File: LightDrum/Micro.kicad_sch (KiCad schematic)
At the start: 14 parts, among them J902 JTAG, SW902 BOOT0, U901 24LC04, Y901 16MHz

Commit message: Add RTC
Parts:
- added C1, C2: 15pF, Capacitor_SMD:C_0402_1005Metric, symbol Daxxn_Device:C
- added Y32: 32.768KHz, Crystal:Crystal_SMD_3215-2Pin_3.2x1.5mm, symbol Daxxn_Device:Crystal_Floating
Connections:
- net GND: now also C1.2, C2.1
- net at STM101.8 (PC14/OSC32-IN): now also C1.1, Y32.1
- net at STM101.9 (PC15/OSC32-OUT): now also C2.2, Y32.2
- no-connect marks 26 -> 24
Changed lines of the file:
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@@
   (junction (at 53.34 93.98) (diameter 0) (color 0 0 0 0)
   )
+  (junction (at 156.21 67.31) (diameter 0) (color 0 0 0 0)
+  )
   (junction (at 49.53 91.44) (diameter 0) (color 0 0 0 0)
   )
+  (junction (at 156.21 72.39) (diameter 0) (color 0 0 0 0)
+  )
   (junction (at 256.54 152.4) (diameter 0) (color 0 0 0 0)
   )
   (junction (at 262.89 71.12) (diameter 0) (color 0 0 0 0)
+  )
+  (junction (at 168.91 72.39) (diameter 0) (color 0 0 0 0)
   )
   (no_connect (at 129.54 78.74))
@@
   (no_connect (at 86.36 60.96))
   (no_connect (at 86.36 71.12))
-  (no_connect (at 129.54 71.12))
   (no_connect (at 86.36 134.62))
   (no_connect (at 86.36 137.16))
@@
   (no_connect (at 129.54 81.28))
   (no_connect (at 129.54 127))
-  (no_connect (at 129.54 68.58))
   (no_connect (at 129.54 33.02))
   (polyline (pts (xy 284.48 134.62) (xy 208.28 134.62))
@@
     (stroke (width 0) (type default))
   )
+  (wire (pts (xy 156.21 67.31) (xy 162.56 67.31))
+    (stroke (width 0) (type default))
+  )
   (wire (pts (xy 233.68 153.67) (xy 233.68 152.4))
     (stroke (width 0) (type default))
@@
     (stroke (width 0) (type default))
   )
+  (wire (pts (xy 129.54 68.58) (xy 149.86 68.58))
+    (stroke (width 0) (type default))
+  )
   (wire (pts (xy 262.89 69.85) (xy 262.89 71.12))
     (stroke (width 0) (type default))
@@
     (stroke (width 0) (type default))
   )
+  (wire (pts (xy 149.86 72.39) (xy 149.86 71.12))
+    (stroke (width 0) (type default))
+  )
   (wire (pts (xy 242.57 101.6) (xy 243.84 101.6))
     (stroke (width 0) (type default))
@@
     (stroke (width 0) (type default))
   )
+  (wire (pts (xy 168.91 72.39) (xy 167.64 72.39))
+    (stroke (width 0) (type default))
+  )
   (wire (pts (xy 255.27 149.86) (xy 256.54 149.86))
     (stroke (width 0) (type default))
@@
     (stroke (width 0) (type default))
   )
+  (wire (pts (xy 168.91 67.31) (xy 168.91 72.39))
+    (stroke (width 0) (type default))
+  )
   (wire (pts (xy 220.98 34.29) (xy 232.41 34.29))
     (stroke (width 0) (type default))
@@
     (stroke (width 0) (type default))
   )
+  (wire (pts (xy 167.64 67.31) (xy 168.91 67.31))
+    (stroke (width 0) (type default))
+  )
   (wire (pts (xy 86.36 101.6) (xy 83.82 101.6))
     (stroke (width 0) (type default))
@@
     (stroke (width 0) (type default))
   )
+  (wire (pts (xy 149.86 68.58) (xy 149.86 67.31))
+    (stroke (width 0) (type default))
+  )
+  (wire (pts (xy 156.21 72.39) (xy 162.56 72.39))
+    (stroke (width 0) (type default))
+  )
+  (wire (pts (xy 168.91 72.39) (xy 168.91 73.66))
+    (stroke (width 0) (type default))
+  )
   (wire (pts (xy 256.54 157.48) (xy 245.11 157.48))
     (stroke (width 0) (type default))
@@
     (stroke (width 0) (type default))
   )
+  (wire (pts (xy 156.21 72.39) (xy 149.86 72.39))
+    (stroke (width 0) (type default))
+  )
   (polyline (pts (xy 208.28 16.51) (xy 236.22 16.51))
     (stroke (width 0) (type default))
@@
     (stroke (width 0) (type default))
   )
+  (wire (pts (xy 149.86 71.12) (xy 129.54 71.12))
+    (stroke (width 0) (type default))
+  )
   (polyline (pts (xy 208.28 86.36) (xy 246.38 86.36))
     (stroke (width 0) (type default))
@@
   )
   (wire (pts (xy 49.53 83.82) (xy 49.53 85.09))
+    (stroke (width 0) (type default))
+  )
+  (wire (pts (xy 149.86 67.31) (xy 156.21 67.31))
     (stroke (width 0) (type default))
   )
@@
     )
   )
+  (symbol (lib_id "Daxxn_Device:C") (at 165.1 72.39 270) (unit 1)
+    (in_bom yes) (on_board yes) (dnp no)
+    (property "Reference" "C2" (at 166.624 72.644 0)
+      (effects (font (size 1.27 1.27)) (justify left))
+    )
+    (property "Value" "15pF" (at 163.195 72.644 0)
+      (effects (font (size 1.27 1.27)) (justify left))
+    )
+    (property "Footprint" "Capacitor_SMD:C_0402_1005Metric" (at 165.1 72.39 0)
+      (effects (font (size 1.27 1.27)) hide)
+    )
+    (property "Datasheet" "~" (at 165.1 72.39 0)
+      (effects (font (size 1.27 1.27)) hide)
+    )
+    (property "Schematic" "" (at 165.1 72.39 0)
+      (effects (font (size 1.27 1.27)) hide)
+    )
+    (property "PartNumber" "" (at 165.1 72.39 0)
+      (effects (font (size 1.27 1.27)))
+    )
+    (property "SupplierPN" "" (at 165.1 72.39 0)
+      (effects (font (size 1.27 1.27)) hide)
+    )
+    (pin "1")
+    (pin "2")
+    (instances
+      (project "LightDrum"
+        (path "/7f137461-fd46-4a4c-8db7-555d487fb3ca/97311934-873d-4d1e-ba68-f7e43f64afbc"
+          (reference "C2") (unit 1)
+        )
+      )
+    )
+  )
   (symbol (lib_id "Device:C_Small") (at 262.89 74.93 0) (unit 1)
     (in_bom yes) (on_board yes) (dnp no)
@@
     )
   )
+  (symbol (lib_id "power:GND") (at 168.91 73.66 0) (unit 1)
+    (in_bom yes) (on_board yes) (dnp no)
+    (property "Reference" "#PWR01" (at 168.91 80.01 0)
+      (effects (font (size 1.27 1.27)) hide)
+    )
+    (property "Value" "GND" (at 168.91 77.47 0)
+      (effects (font (size 1.27 1.27)))
+    )
+    (property "Footprint" "" (at 168.91 73.66 0)
+      (effects (font (size 1.27 1.27)) hide)
+    )
+    (property "Datasheet" "" (at 168.91 73.66 0)
+      (effects (font (size 1.27 1.27)) hide)
+    )
+    (pin "1")
+    (instances
+      (project "LightDrum"
+        (path "/7f137461-fd46-4a4c-8db7-555d487fb3ca/97311934-873d-4d1e-ba68-f7e43f64afbc"
+          (reference "#PWR01") (unit 1)
+        )
+      )
+    )
+  )
   (symbol (lib_id "power:VDD") (at 213.36 67.31 0) (unit 1)
     (in_bom yes) (on_board yes) (dnp no)
@@
     )
   )
+  (symbol (lib_id "Daxxn_Device:Crystal_Floating") (at 156.21 69.85 270) (unit 1)
+    (in_bom yes) (on_board yes) (dnp no)
+    (property "Reference" "Y32" (at 160.274 69.85 0)
+      (effects (font (size 1.27 1.27)))
+    )
+    (property "Value" "32.768KHz" (at 158.623 69.85 0)
+      (effects (font (size 1.27 1.27)))
+    )
+    (property "Footprint" "Crystal:Crystal_SMD_3215-2Pin_3.2x1.5mm" (at 156.21 69.85 0)
+      (effects (font (size 1.27 1.27)) hide)
+    )
+    (property "Datasheet" "https://ecsxtal.com/store/pdf/ecx-31b.pdf" (at 156.21 69.85 0)
+      (effects (font (size 1.27 1.27)) hide)
+    )
+    (property "Schematic" "" (at 156.21 69.85 0)
+      (effects (font (size 1.27 1.27)) hide)
+    )
+    (property "PartNumber" "" (at 156.21 69.85 0)
+      (effects (font (size 1.27 1.27)))
+    )
+    (property "SupplierPN" "" (at 156.21 69.85 0)
+      (effects (font (size 1.27 1.27)) hide)
+    )
+    (pin "1")
+    (pin "2")
+    (instances
+      (project "LightDrum"
+        (path "/7f137461-fd46-4a4c-8db7-555d487fb3ca/97311934-873d-4d1e-ba68-f7e43f64afbc"
+          (reference "Y32") (unit 1)
+        )
+      )
+    )
+  )
   (symbol (lib_id "Device:R_Small_US") (at 228.6 39.37 270) (unit 1)
     (in_bom yes) (on_board yes) (dnp no)
@@
         )
       )
+    )
+  )
+  (symbol (lib_id "Daxxn_Device:C") (at 165.1 67.31 90) (unit 1)
+    (in_bom yes) (on_board yes) (dnp no)
+    (property "Reference" "C1" (at 163.576 67.056 0)
+      (effects (font (size 1.27 1.27)) (justify left))
+    )
+    (property "Value" "15pF" (at 167.005 67.056 0)
+      (effects (font (size 1.27 1.27)) (justify left))
+    )
+    (property "Footprint" "Capacitor_SMD:C_0402_1005Metric" (at 165.1 67.31 0)
+      (effects (font (size 1.27 1.27)) hide)
+    )
+    (property "Datasheet" "~" (at 165.1 67.31 0)
+      (effects (font (size 1.27 1.27)) hide)
+    )
+    (property "Schematic" "" (at 165.1 67.31 0)
+      (effects (font (size 1.27 1.27)) hide)
+    )
+    (property "PartNumber" "" (at 165.1 67.31 0)
+      (effects (font (size 1.27 1.27)))
+    )
+    (property "SupplierPN" "" (at 165.1 67.31 0)
+      (effects (font (size 1.27 1.27)) hide)
+    )
+    (pin "1")
+    (pin "2")
+    (instances
+      (project "LightDrum"
+        (path "/7f137461-fd46-4a4c-8db7-555d487fb3ca/97311934-873d-4d1e-ba68-f7e43f64afbc"
+          (reference "C1") (unit 1)
+        )
+      )

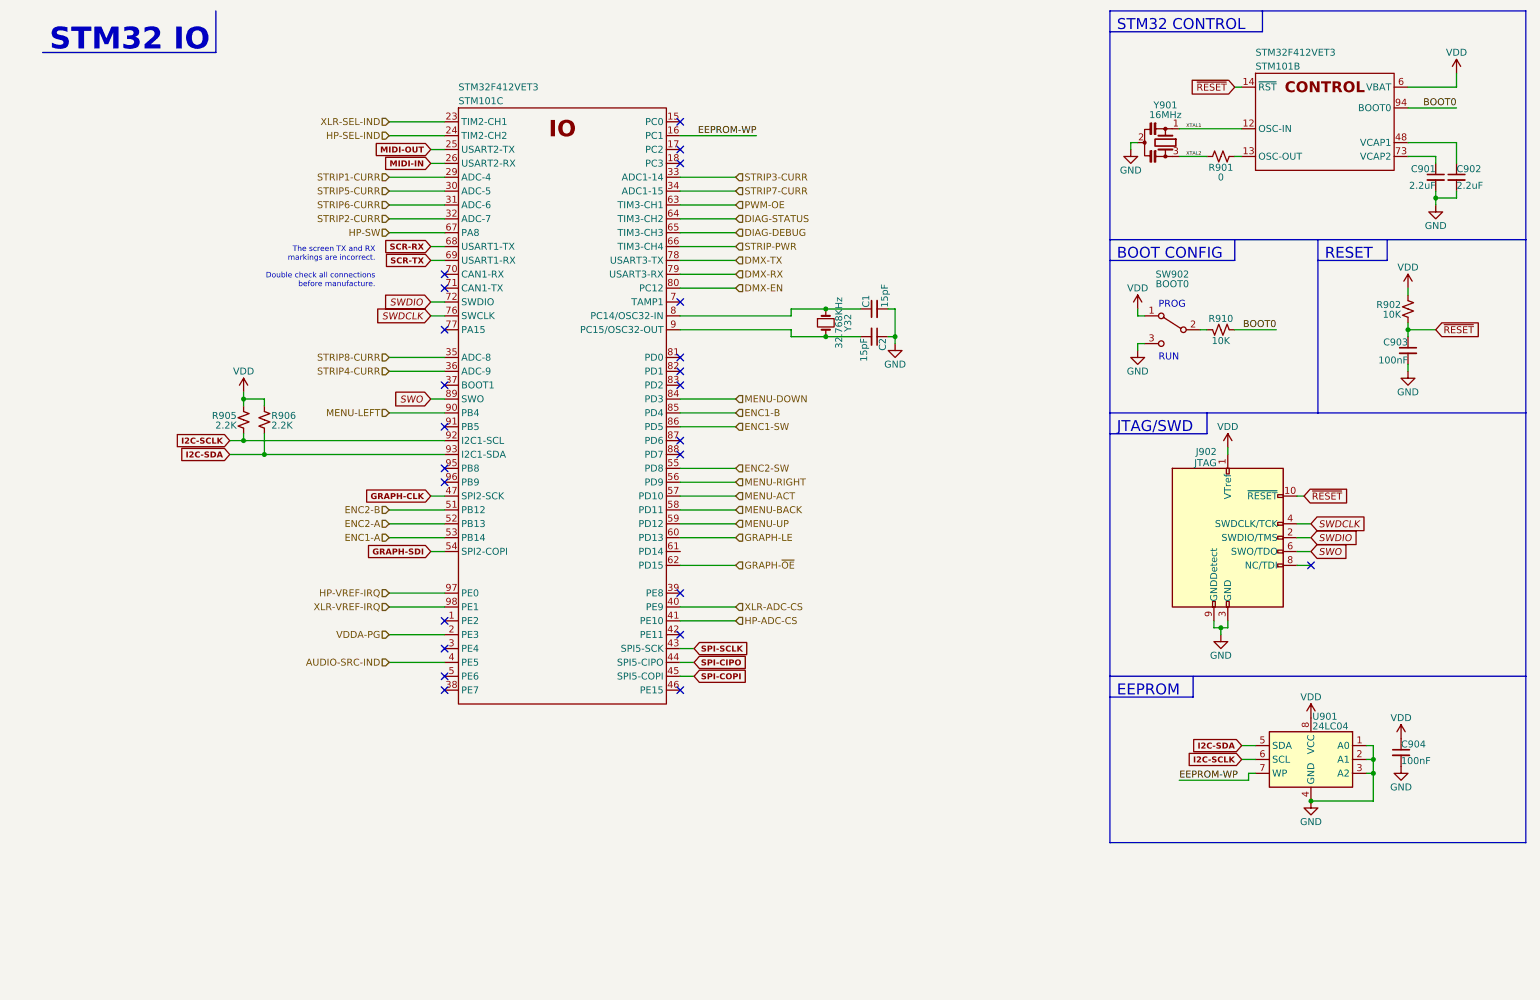
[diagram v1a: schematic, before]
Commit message: Replace relays and SWD conn
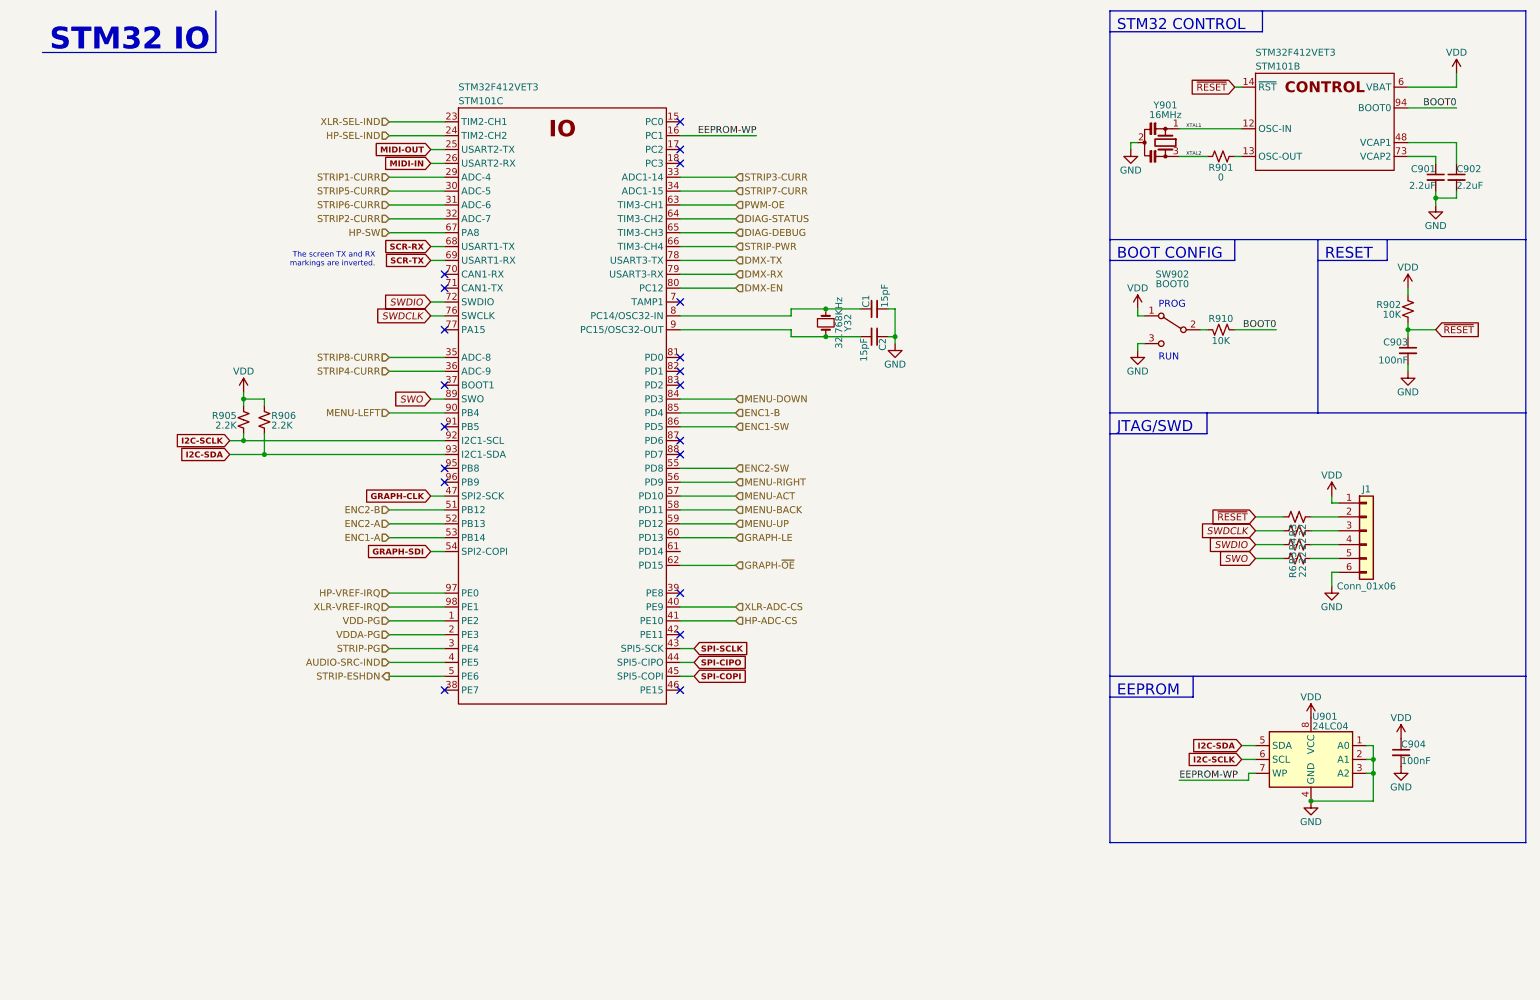
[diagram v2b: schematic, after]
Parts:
- removed J902: JTAG, Connector:Tag-Connect_TC2050-IDC-FP_2x05_P1.27mm_Vertical, symbol Connector:Conn_ARM_JTAG_SWD_10
- added J1: Conn_01x06, Connector_PinHeader_1.27mm:PinHeader_1x06_P1.27mm_Vertical, symbol Connector_Generic:Conn_01x06
- added R3, R4, R5, R6: 22, Resistor_SMD:R_0402_1005Metric, symbol Device:R_Small_US
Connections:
- net GND: now also J1.6 (Pin_6)
- net SWDCLK: now also R4.1
- net SWDIO: now also R5.1
- net SWO: now also R6.1
- net VDD: now also J1.1 (Pin_1)
- net ~{RESET}: now also R3.1
- net VDD-PG: now reaches STM101.1 (PE2)
- net STRIP-PG: now reaches STM101.3 (PE4)
- net STRIP-ESHDN: now reaches STM101.5 (PE6)
- new net: J1.2 (Pin_2), R3.2
- new net: J1.3 (Pin_3), R4.2
- new net: J1.4 (Pin_4), R5.2
- new net: J1.5 (Pin_5), R6.2
- no-connect marks 24 -> 20
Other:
- note added: "The screen TX and RX markings are inverted."
- note removed: "The screen TX and RX markings are incorrect. Double check all connections before manufacture."

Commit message: Preliminary schematic lock - Starting PCB layout
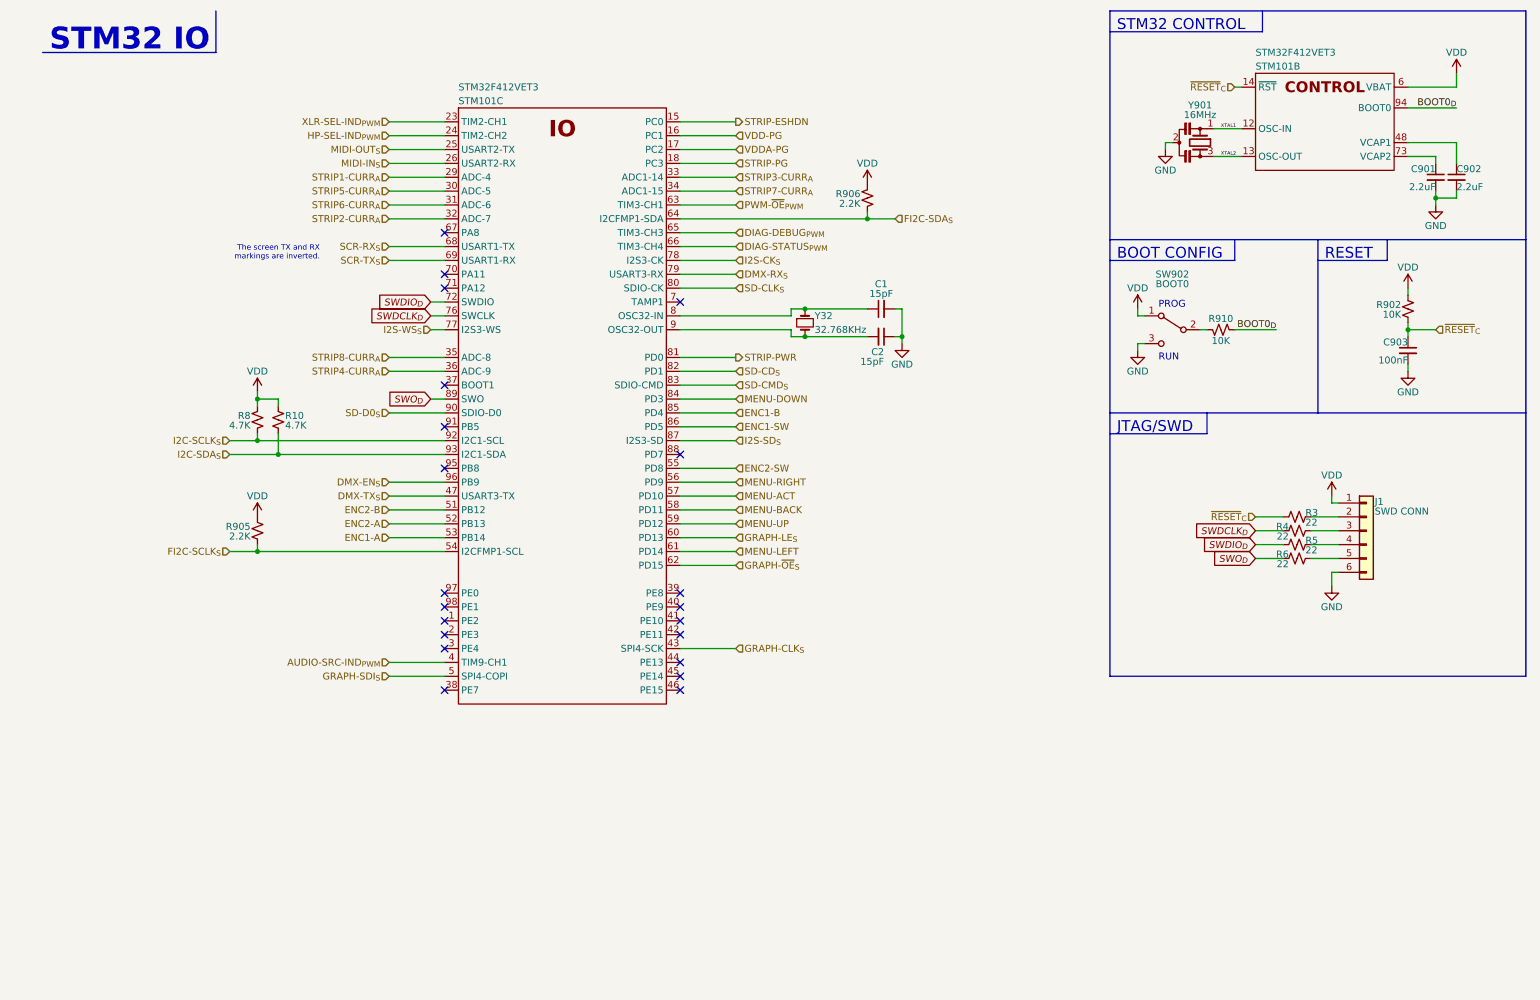
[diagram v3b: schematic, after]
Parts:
- removed C904: 100nF, Capacitor_SMD:C_0402_1005Metric, symbol Device:C_Small
- removed R901: 0, Resistor_SMD:R_0402_1005Metric, symbol Device:R_Small_US
- removed U901: 24LC04, Package_SO:SOIC-8_3.9x4.9mm_P1.27mm, symbol Memory_EEPROM:24LC04
- added R10, R8: 4.7K, Resistor_SMD:R_0402_1005Metric, symbol Device:R_Small_US
- C1, C2: SupplierPN (none) -> 399-C0402C150G5HACAUTOCT-ND
- C901, C902: footprint Capacitor_SMD:C_0603_1608Metric -> Capacitor_SMD:C_0402_1005Metric; SupplierPN (none) -> 478-11437-1-ND
- C903: SupplierPN (none) -> 1276-1043-1-ND
- J1: value Conn_01x06 -> SWD CONN; SupplierPN (none) -> 952-3602-ND
- R3, R4, R5, R6: SupplierPN (none) -> 2037-PFR05S-220-FNHCT-ND
- R902, R910: SupplierPN (none) -> 311-10KJRCT-ND
- R905, R906: SupplierPN (none) -> 311-2.2KJRCT-ND
- STM101: SupplierPN (none) -> 497-18547-ND
- SW902: SupplierPN (none) -> 401-2016-1-ND
- Y32: SupplierPN (none) -> XC1617CT-ND
- Y901: SupplierPN (none) -> 490-17948-1-ND
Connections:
- net EEPROM-WP is gone; now on net VDD-PG: STM101.16 (PC1)
- net MENU-LEFT: now also STM101.61 (PD14); no longer STM101.90 (PB4)
- net STRIP-ESHDN: now also STM101.15 (PC0); no longer STM101.5 (PE6)
- net STRIP-PG: now also STM101.18 (PC3); no longer STM101.3 (PE4)
- net STRIP-PWR: now also STM101.81 (PD0); no longer STM101.66 (PC9)
- net VDD: now also R10.1, R8.1
- net VDD-PG: no longer STM101.1 (PE2)
- net VDDA-PG: now also STM101.17 (PC2); no longer STM101.2 (PE3)
- net XTAL2: now also STM101.13 (OSC-OUT)
- net I2S-WS_{S}: now reaches STM101.77 (PA15)
- net SD-CD_{S}: now reaches STM101.82 (PD1)
- net SD-CMD_{S}: now reaches STM101.83 (PD2)
- net I2S-SD_{S}: now reaches STM101.87 (PD6)
- net DMX-EN_{S}: now reaches STM101.96 (PB9)
- net AUDIO-SRC-IND renamed AUDIO-SRC-IND_{PWM}
- net BOOT0 renamed BOOT0_{D}
- net DIAG-DEBUG renamed DIAG-DEBUG_{PWM}
- net DIAG-STATUS renamed FI2C-SDA_{S}
- net FI2C-SDA_{S}: now also R906.2
- net DMX-EN renamed SD-CLK_{S}
- net DMX-RX renamed DMX-RX_{S}
- net DMX-TX renamed I2S-CK_{S}
- net GRAPH-CLK renamed DMX-TX_{S}
- net GRAPH-LE renamed GRAPH-LE_{S}
- net GRAPH-SDI renamed FI2C-SCLK_{S}
- net FI2C-SCLK_{S}: now also R905.2
- net GRAPH-~{OE} renamed GRAPH-~{OE}_{S}
- net HP-ADC-CS: no longer names the net of STM101.41 (PE10)
- net HP-SEL-IND renamed HP-SEL-IND_{PWM}
- net HP-SW: no longer names the net of STM101.67 (PA8)
- net HP-VREF-IRQ: no longer names the net of STM101.97 (PE0)
- net I2C-SCLK renamed I2C-SCLK_{S}
- net I2C-SCLK_{S}: now also R8.2; no longer R905.2
- net I2C-SDA renamed I2C-SDA_{S}
- net I2C-SDA_{S}: now also R10.2; no longer R906.2
- net MIDI-IN renamed MIDI-IN_{S}
- net MIDI-OUT renamed MIDI-OUT_{S}
- net PWM-OE renamed PWM-~{OE}_{PWM}
- net SCR-RX renamed SCR-RX_{S}
- net SCR-TX renamed SCR-TX_{S}
- net SPI-CIPO: no longer names the net of STM101.44 (PE13)
- net SPI-COPI: no longer names the net of STM101.45 (PE14)
- net SPI-SCLK renamed GRAPH-CLK_{S}
- net STRIP1-CURR renamed STRIP1-CURR_{A}
- net STRIP2-CURR renamed STRIP2-CURR_{A}
- net STRIP3-CURR renamed STRIP3-CURR_{A}
- net STRIP4-CURR renamed STRIP4-CURR_{A}
- net STRIP5-CURR renamed STRIP5-CURR_{A}
- net STRIP6-CURR renamed STRIP6-CURR_{A}
- net STRIP7-CURR renamed STRIP7-CURR_{A}
- net STRIP8-CURR renamed STRIP8-CURR_{A}
- net SWDCLK renamed SWDCLK_{D}
- net SWDIO renamed SWDIO_{D}
- net SWO renamed SWO_{D}
- net XLR-ADC-CS: no longer names the net of STM101.40 (PE9)
- net XLR-SEL-IND renamed XLR-SEL-IND_{PWM}
- net XLR-VREF-IRQ: no longer names the net of STM101.98 (PE1)
- net ~{RESET} renamed ~{RESET}_{C}
- new net DIAG-STATUS_{PWM}: STM101.66 (PC9)
- new net GRAPH-SDI_{S}: STM101.5 (PE6)
- new net SD-D0_{S}: STM101.90 (PB4)
- no-connect marks 20 -> 21
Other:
- note removed: "EEPROM"
- moved on the sheet: C1, C2, R905, R906, Y32, Y901
